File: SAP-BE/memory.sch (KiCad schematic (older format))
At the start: 33 parts, among them SW3 SW_DIP_x08, SW4 SW_SPDT, SW5 SW_DIP_x04, SW6 SW_Push, U32 74LS04, U35 74LS173, U36 74LS157, U37 74LS157, U38 74LS189, U39 74LS189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

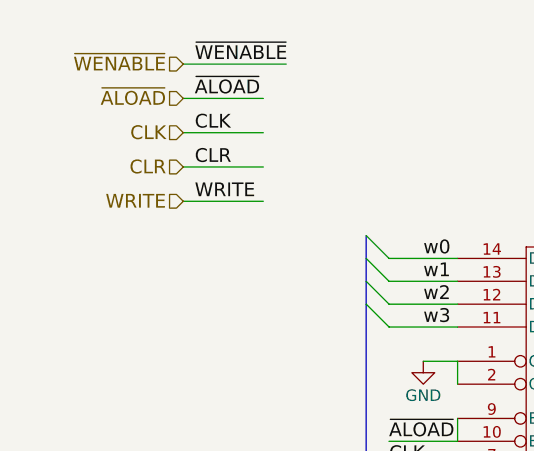
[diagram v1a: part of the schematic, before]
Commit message: Update with changes for reset
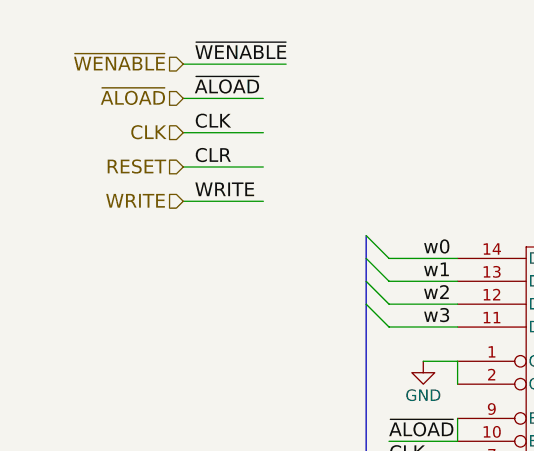
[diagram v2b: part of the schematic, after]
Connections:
- net labels added: RESET
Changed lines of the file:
@@
 	8150 5400 8250 5500
 $Comp
-L VCC #PWR52
+L VCC #PWR040
 U 1 1 5914B8BD
 P 8550 5700
-F 0 "#PWR52" H 8550 5550 50  0001 C CNN
+F 0 "#PWR040" H 8550 5550 50  0001 C CNN
 F 1 "VCC" H 8550 5850 50  0000 C CNN
 F 2 "" H 8550 5700 50  0000 C CNN
@@
 $EndComp
 $Comp
-L GND #PWR44
+L GND #PWR041
 U 1 1 5914F2ED
 P 3050 3350
-F 0 "#PWR44" H 3050 3100 50  0001 C CNN
+F 0 "#PWR041" H 3050 3100 50  0001 C CNN
 F 1 "GND" H 3050 3200 50  0000 C CNN
 F 2 "" H 3050 3350 50  0000 C CNN
@@
 a3
 $Comp
-L GND #PWR43
+L GND #PWR042
 U 1 1 59152977
 P 3050 1400
-F 0 "#PWR43" H 3050 1150 50  0001 C CNN
+F 0 "#PWR042" H 3050 1150 50  0001 C CNN
 F 1 "GND" H 3050 1250 50  0000 C CNN
 F 2 "" H 3050 1400 50  0000 C CNN
@@
 	4200 2900 4200 2950
 $Comp
-L VCC #PWR45
+L VCC #PWR043
 U 1 1 591534A9
 P 4050 2550
-F 0 "#PWR45" H 4050 2400 50  0001 C CNN
+F 0 "#PWR043" H 4050 2400 50  0001 C CNN
 F 1 "VCC" H 4050 2700 50  0000 C CNN
 F 2 "" H 4050 2550 50  0000 C CNN
@@
 	4250 1200 3750 1200
 $Comp
-L GND #PWR48
+L GND #PWR044
 U 1 1 59153EEF
 P 4900 2300
-F 0 "#PWR48" H 4900 2050 50  0001 C CNN
+F 0 "#PWR044" H 4900 2050 50  0001 C CNN
 F 1 "GND" H 4900 2150 50  0000 C CNN
 F 2 "" H 4900 2300 50  0000 C CNN
@@
 	2350 2200 2350 2300
 $Comp
-L GND #PWR40
+L GND #PWR045
 U 1 1 59155C0A
 P 2200 2200
-F 0 "#PWR40" H 2200 1950 50  0001 C CNN
+F 0 "#PWR045" H 2200 1950 50  0001 C CNN
 F 1 "GND" H 2200 2050 50  0000 C CNN
 F 2 "" H 2200 2200 50  0000 C CNN
@@
 Text Label 2050 2850 0    60   ~ 0
 CLR
-Text HLabel 1150 1350 0    60   Input ~ 0
-CLR
 Wire Wire Line
 	1150 1350 1500 1350
@@
 $EndComp
 $Comp
-L GND #PWR49
+L GND #PWR046
 U 1 1 5915F5BE
 P 5850 3400
-F 0 "#PWR49" H 5850 3150 50  0001 C CNN
+F 0 "#PWR046" H 5850 3150 50  0001 C CNN
 F 1 "GND" H 5850 3250 50  0000 C CNN
 F 2 "" H 5850 3400 50  0000 C CNN
@@
 $EndComp
 $Comp
-L GND #PWR39
+L GND #PWR047
 U 1 1 5916EDB7
 P 700 5600
-F 0 "#PWR39" H 700 5350 50  0001 C CNN
+F 0 "#PWR047" H 700 5350 50  0001 C CNN
 F 1 "GND" H 700 5450 50  0000 C CNN
 F 2 "" H 700 5600 50  0000 C CNN
@@
 Connection ~ 700  5350
 $Comp
-L GND #PWR41
+L GND #PWR048
 U 1 1 5917082B
 P 2250 5250
-F 0 "#PWR41" H 2250 5000 50  0001 C CNN
+F 0 "#PWR048" H 2250 5000 50  0001 C CNN
 F 1 "GND" H 2250 5100 50  0000 C CNN
 F 2 "" H 2250 5250 50  0000 C CNN
@@
 $EndComp
 $Comp
-L GND #PWR42
+L GND #PWR049
 U 1 1 59170E71
 P 2250 6750
-F 0 "#PWR42" H 2250 6500 50  0001 C CNN
+F 0 "#PWR049" H 2250 6500 50  0001 C CNN
 F 1 "GND" H 2250 6600 50  0000 C CNN
 F 2 "" H 2250 6750 50  0000 C CNN
@@
 $EndComp
 $Comp
-L GND #PWR51
+L GND #PWR050
 U 1 1 591761D7
 P 8150 3450
-F 0 "#PWR51" H 8150 3200 50  0001 C CNN
+F 0 "#PWR050" H 8150 3200 50  0001 C CNN
 F 1 "GND" H 8150 3300 50  0000 C CNN
 F 2 "" H 8150 3450 50  0000 C CNN
@@
 $EndComp
 $Comp
-L GND #PWR46
+L GND #PWR051
 U 1 1 5918B299
 P 4550 4950
-F 0 "#PWR46" H 4550 4700 50  0001 C CNN
+F 0 "#PWR051" H 4550 4700 50  0001 C CNN
 F 1 "GND" H 4550 4800 50  0000 C CNN
 F 2 "" H 4550 4950 50  0000 C CNN
@@
 	4550 4950 4650 4950
 $Comp
-L GND #PWR47
+L GND #PWR052
 U 1 1 5918BC6E
 P 4550 6450
-F 0 "#PWR47" H 4550 6200 50  0001 C CNN
+F 0 "#PWR052" H 4550 6200 50  0001 C CNN
 F 1 "GND" H 4550 6300 50  0000 C CNN
 F 2 "" H 4550 6450 50  0000 C CNN
@@
 ~WE
 $Comp
-L GND #PWR54
+L GND #PWR053
 U 1 1 5918F2A7
 P 9100 2350
-F 0 "#PWR54" H 9100 2100 50  0001 C CNN
+F 0 "#PWR053" H 9100 2100 50  0001 C CNN
 F 1 "GND" H 9100 2200 50  0000 C CNN
 F 2 "" H 9100 2350 50  0000 C CNN
@@
 	9100 2350 9250 2350
 $Comp
-L GND #PWR53
+L GND #PWR054
 U 1 1 5918F41E
 P 8600 850
-F 0 "#PWR53" H 8600 600 50  0001 C CNN
+F 0 "#PWR054" H 8600 600 50  0001 C CNN
 F 1 "GND" H 8600 700 50  0000 C CNN
 F 2 "" H 8600 850 50  0000 C CNN
@@
 NoConn ~ 10750 2050
 $Comp
-L GND #PWR50
+L GND #PWR055
 U 1 1 5918268B
 P 7850 1850
-F 0 "#PWR50" H 7850 1600 50  0001 C CNN
+F 0 "#PWR055" H 7850 1600 50  0001 C CNN
 F 1 "GND" H 7850 1700 50  0000 C CNN
 F 2 "" H 7850 1850 50  0000 C CNN
@@
 	1    0    0    -1
 $EndComp
+Text HLabel 1150 1350 0    60   Input ~ 0
+RESET
 $EndSCHEMATC

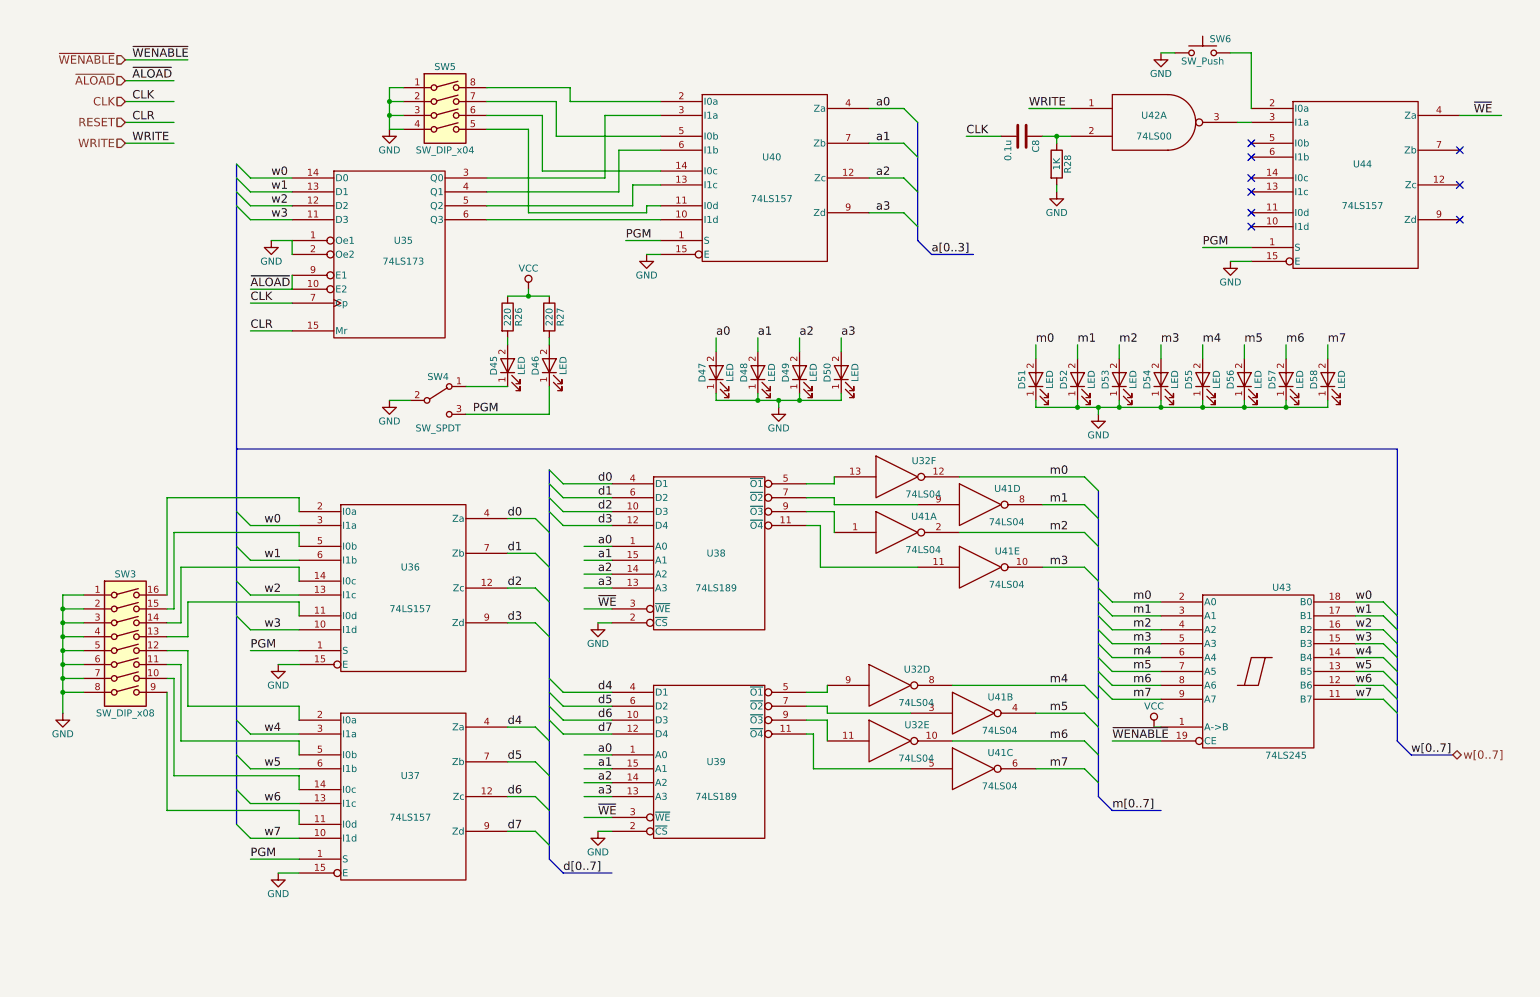
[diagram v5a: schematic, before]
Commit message: Improve memory schematic layout
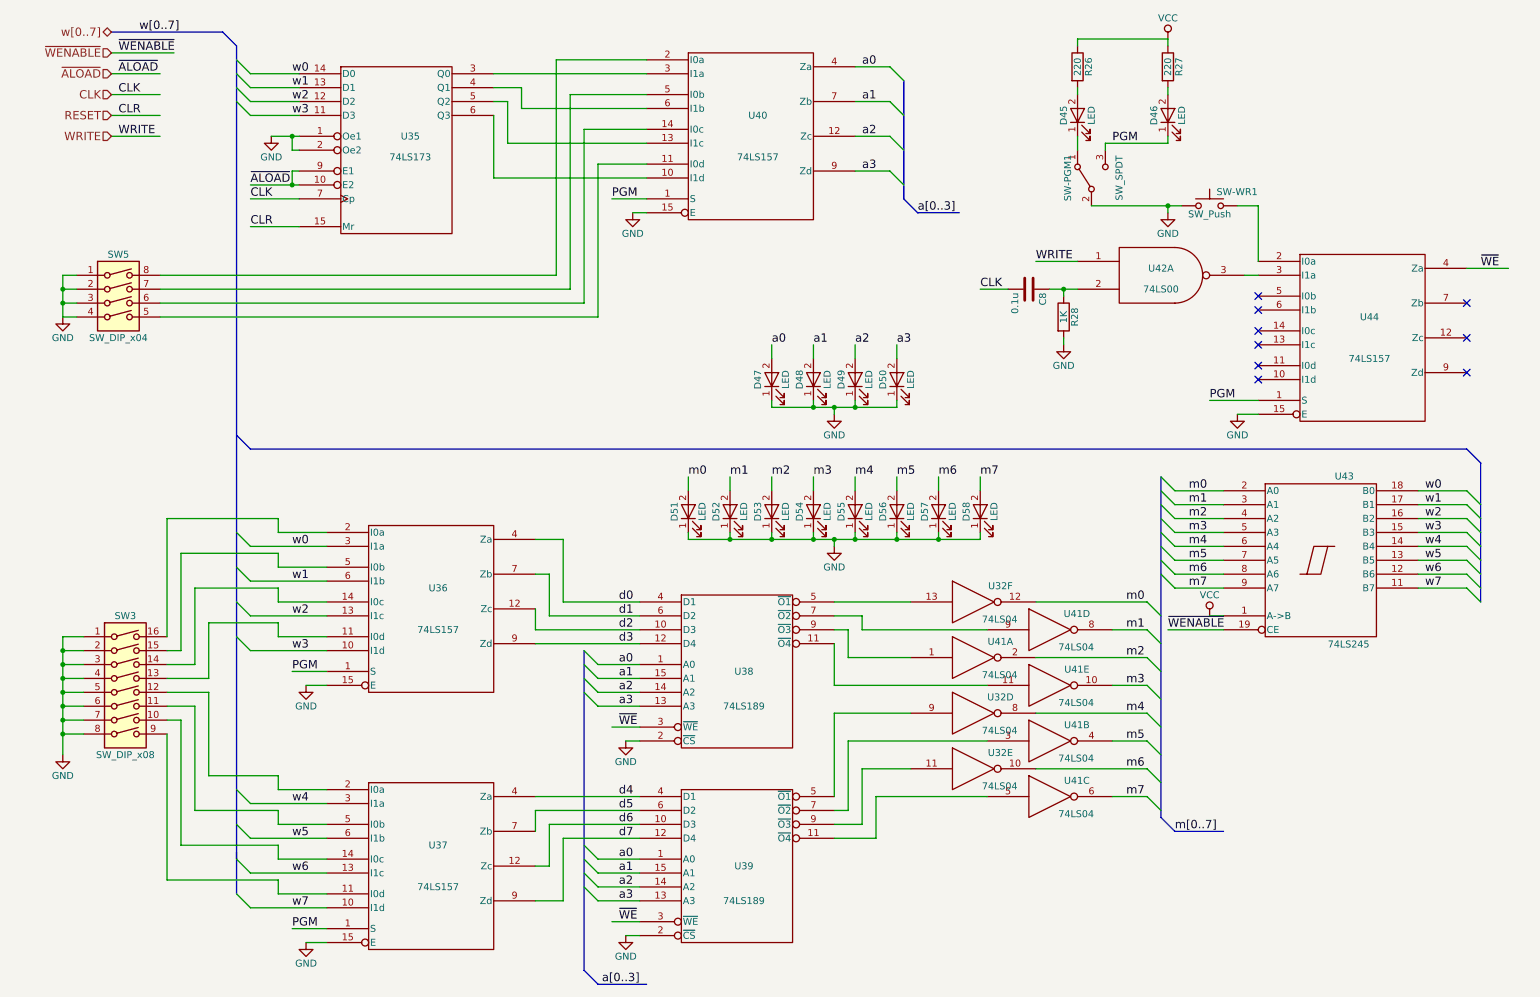
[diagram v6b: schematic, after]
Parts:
- renumbered SW4 to SW-PGM1, SW6 to SW-WR1
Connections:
- net labels removed: d[0..7]
- wire segments 223 -> 234
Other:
- moved on the sheet: C8, D45, D46, D47, D48, D49, D50, D51, D52, D53, D54, D55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

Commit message: clean up memory module schematic a bit
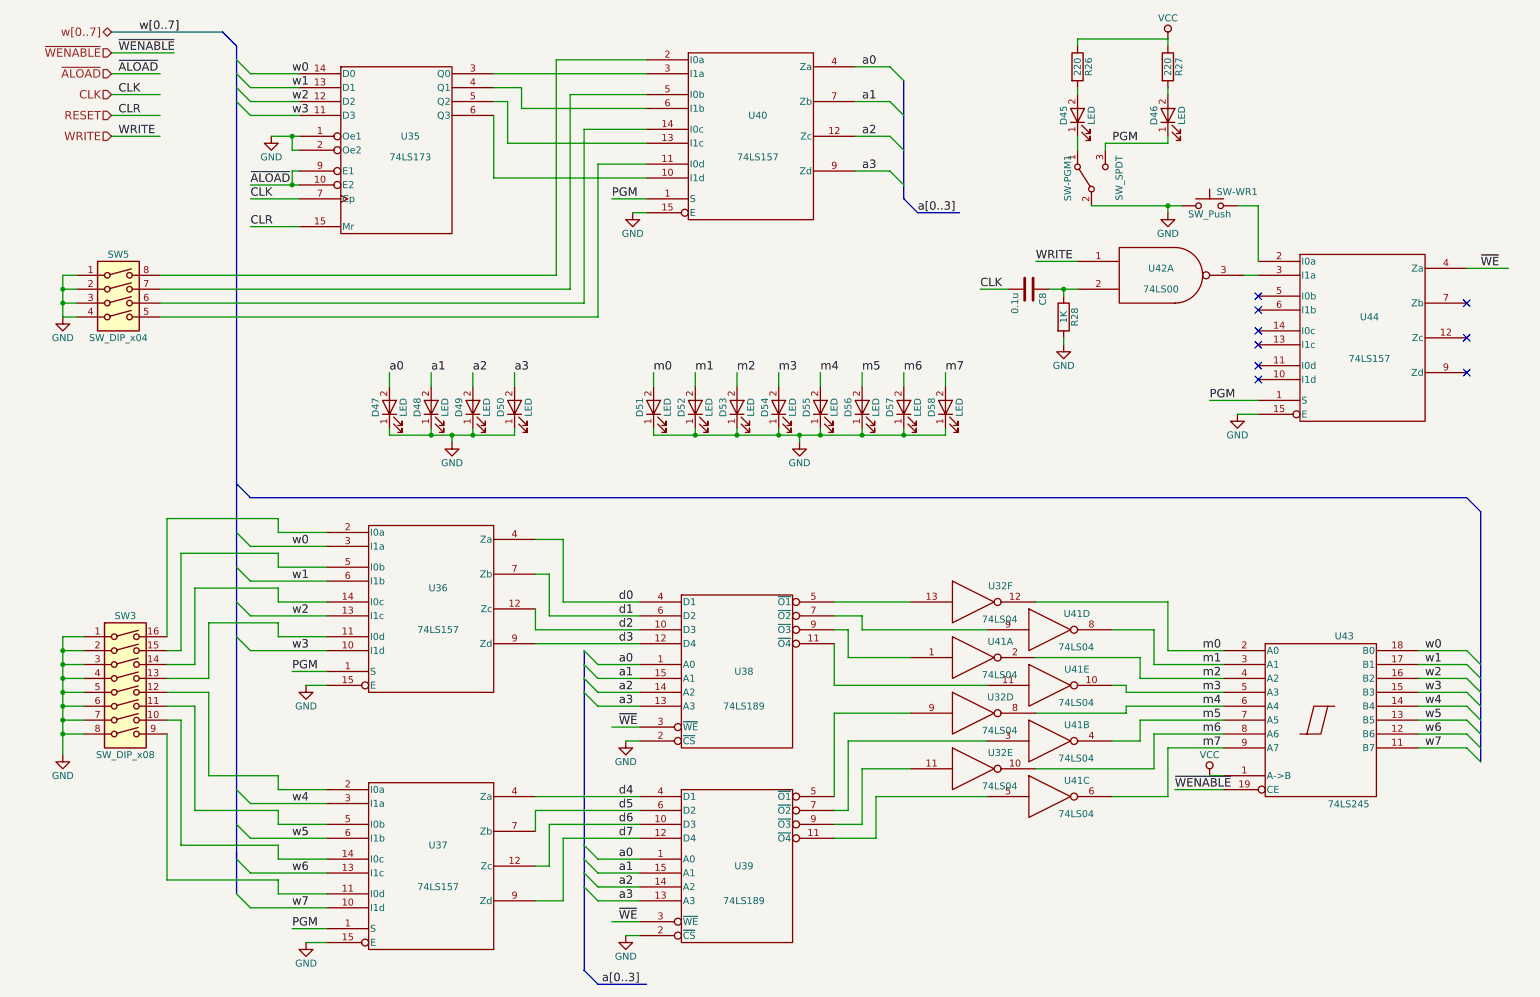
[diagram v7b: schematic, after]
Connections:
- net labels removed: m[0..7]
- wire segments 234 -> 242
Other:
- moved on the sheet: D47, D48, D49, D50, D51, D52, D53, D54, D55, D56, D57, D58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
